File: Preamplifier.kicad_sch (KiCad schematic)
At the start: 23 parts, among them Q301 2N3906, Q302 2N3906, U301 TL072

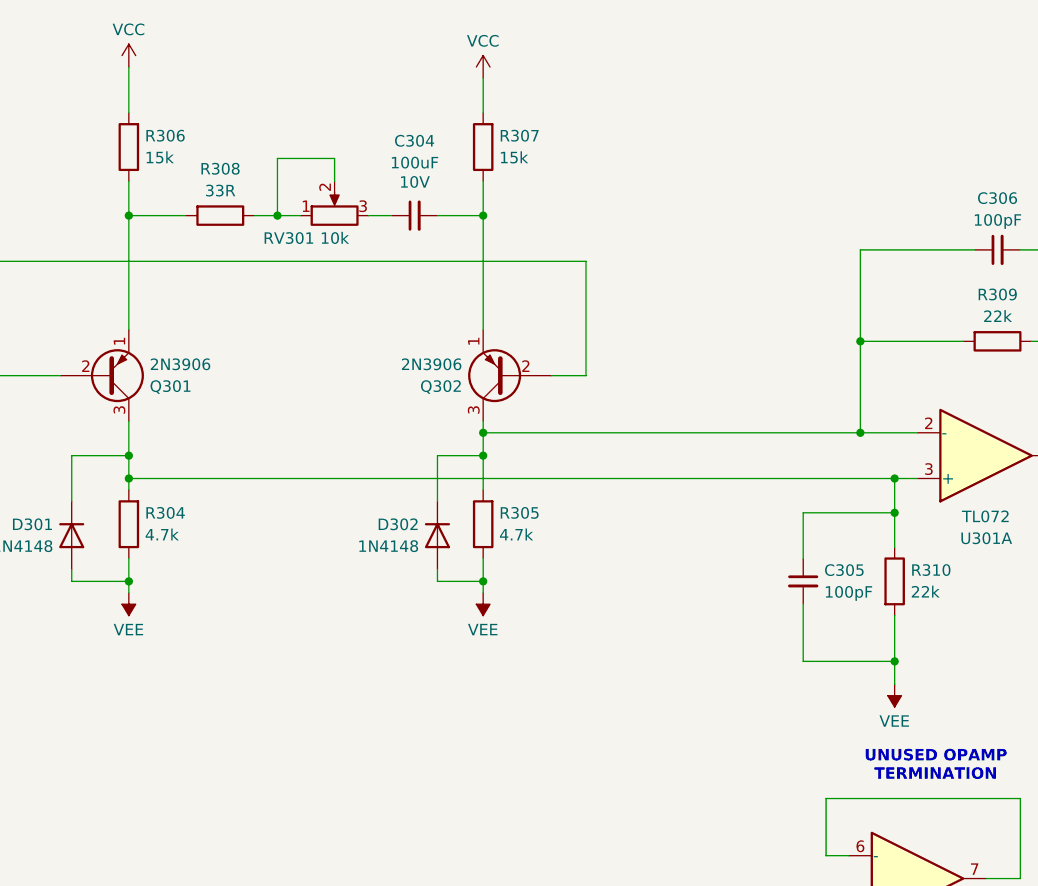
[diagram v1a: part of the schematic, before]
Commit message: Added schematic, assembly drawings, and assembly BoM exports
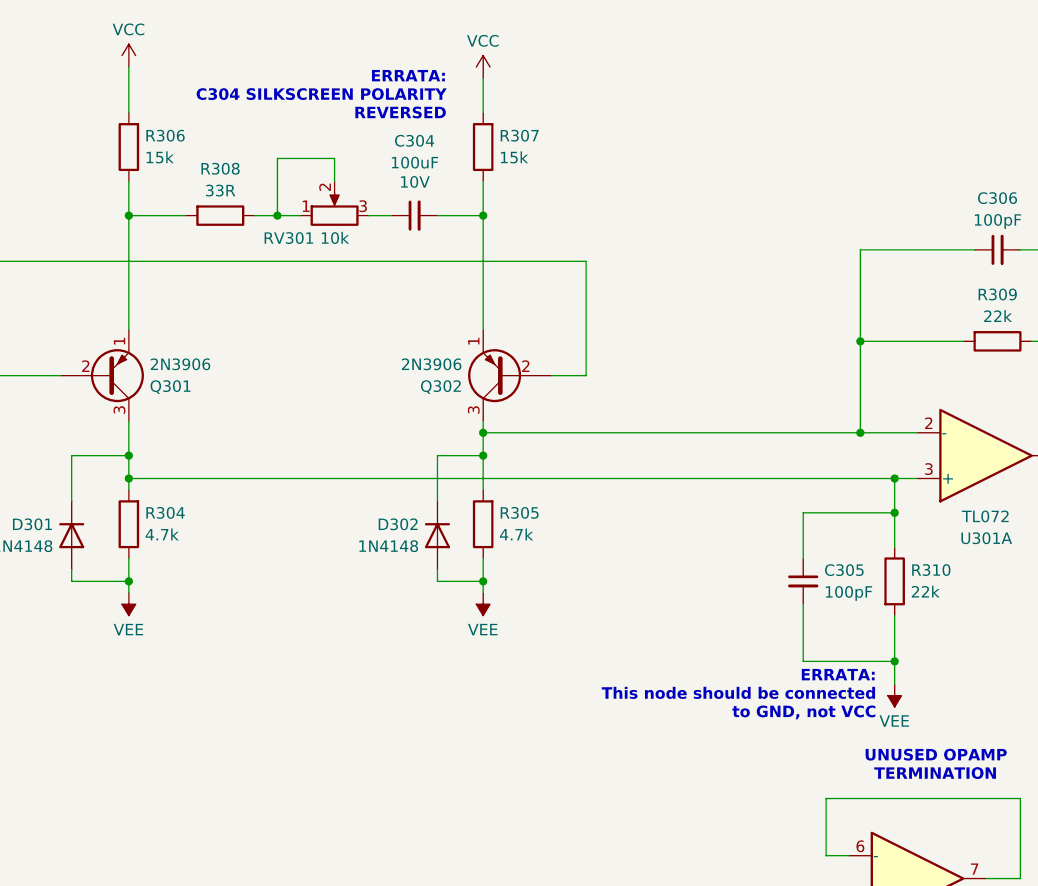
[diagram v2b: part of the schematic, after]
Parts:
- C301: Source (none) -> MOUSER: 810-FG28C0G1H102JNT6
- C302, C303, C304: Source (none) -> MOUSER: 232-25PX100MEFC5X11
- C305, C306: Source (none) -> MOUSER: 810-FG18C0G1H101JNT0
- C307: PartNo. (none) -> MOUSER: 232-25PK47MEFC5X11; Source (none) -> MOUSER: 232-25PK47MEFC5X11
- D301, D302: Source (none) -> MOUSER: 512-1N4148
- Q301, Q302: Source (none) -> MOUSER: 637-2N3906
- R301: Source (none) -> MOUSER: 603-MFR-25FRF52-3K3
- R302, R303: Source (none) -> MOUSER: 603-MFR-25FBF52-47K
- R304, R305: Source (none) -> MOUSER: 603-MFR-25FTF52-4K7
- R306, R307: Source (none) -> MOUSER: 603-MFR-25FRF5215K
- R308: Source (none) -> MOUSER: 603-MFR-25FBF52-33R
- R309, R310: Source (none) -> MOUSER: 603-MFR-25FTF52-22K
- RV301: Source (none) -> MOUSER: 306-B3BXHALFSNP
- U301: Source (none) -> MOUSER: 595-TL072CP
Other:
- note added: "ERRATA: C304 SILKSCREEN POLARITY REVERSED"
- note added: "ERRATA: This node should be connected to GND, not VCC"
